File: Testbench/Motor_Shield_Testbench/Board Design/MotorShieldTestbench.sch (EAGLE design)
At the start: 12 parts

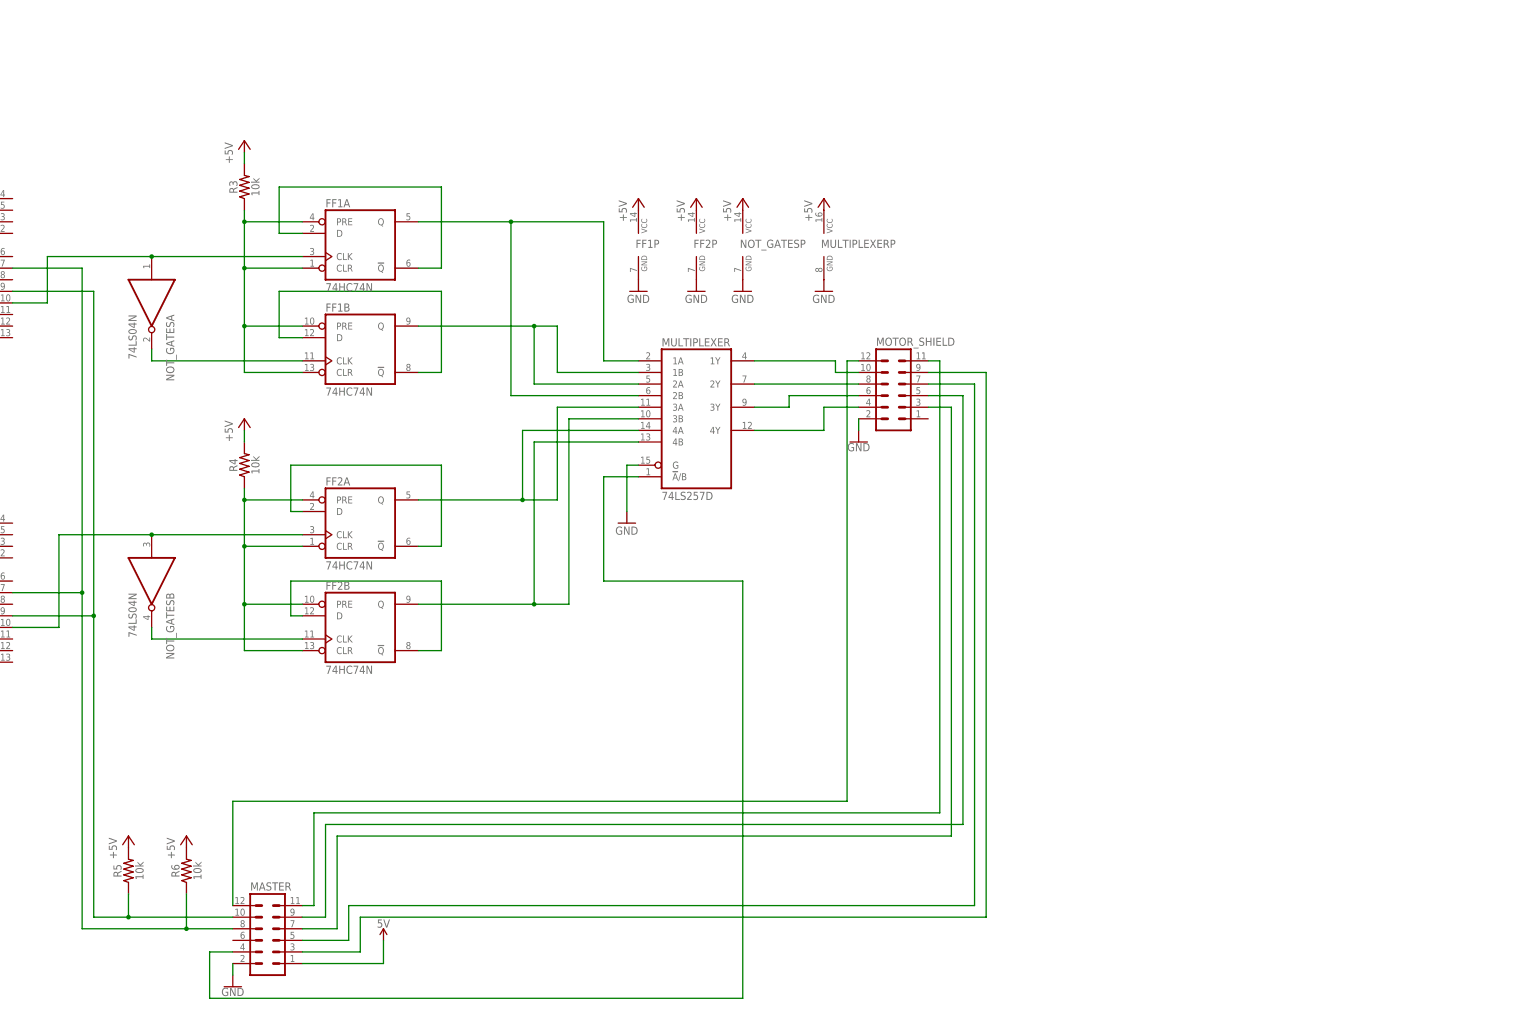
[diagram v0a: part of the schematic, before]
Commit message: board design v2 with complement master pin adjustments
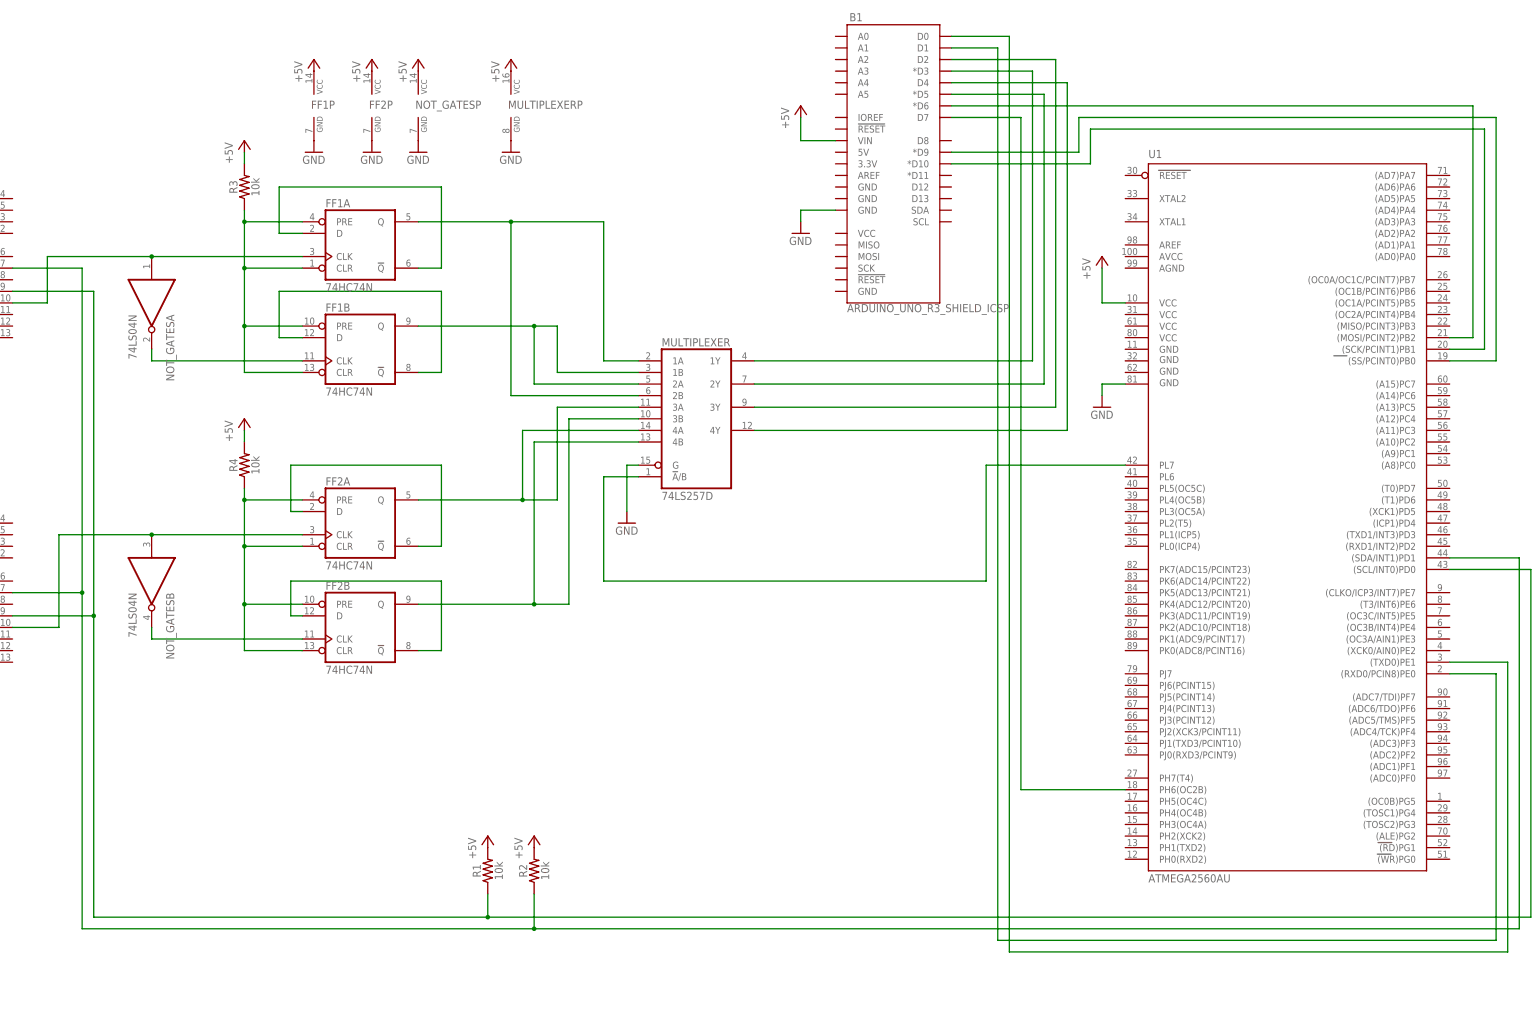
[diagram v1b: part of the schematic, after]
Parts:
- removed MASTER, MOTOR_SHIELD: (no value), con-lstb:MA06-2
- removed R5, R6: 10k, SparkFun-Resistors:10KOHM-HORIZ-1/4W-5%
- added B1: ARDUINO_UNO_R3_SHIELD_ICSP, SparkFun-Boards:ARDUINO_UNO_R3_SHIELD_ICSP
- added R1, R2: 10k, SparkFun-Resistors:10KOHM-HORIZ-1/4W-5%
- added U1: ATMEGA2560AU, SparkFun-IC-Microcontroller:ATMEGA2560AU
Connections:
- removed net 5V: MASTER.1
- removed net N$22: MASTER.7, MOTOR_SHIELD.3
- removed net N$24: MASTER.9, MOTOR_SHIELD.5
- removed net N$25: MASTER.5, MOTOR_SHIELD.7
- removed net N$26: MASTER.3, MOTOR_SHIELD.9
- new net N$28: B1.D0, U1.(TXD0)PE1
- new net N$29: B1.*D9, U1.(SS/PCINT0)PB0
- new net N$30: B1.*D10, U1.(SCK/PCINT1)PB1
- new net N$31: B1.*D6, U1.(MOSI/PCINT2)PB2
- net +5V: now also B1.VIN, R1.2, R2.2, U1.VCC; no longer R5.2, R6.2
- net GND: now also B1.GND@0, U1.GND3; no longer MASTER.2, MOTOR_SHIELD.2
- net N$12: now also B1.D1, U1.(RXD0/PCIN8)PE0; no longer MASTER.11, MOTOR_SHIELD.11
- net N$15: now also B1.*D3; no longer MOTOR_SHIELD.10
- net N$16: now also B1.*D5; no longer MOTOR_SHIELD.8
- net N$17: now also B1.D2; no longer MOTOR_SHIELD.6
- net N$18: now also B1.D4; no longer MOTOR_SHIELD.4
- net N$19: now also R1.1, U1.(SCL/INT0)PD0; no longer MASTER.10, R5.1
- net N$20: now also U1.PL7; no longer MASTER.4
- net N$21: now also R2.1, U1.(SDA/INT1)PD1; no longer MASTER.8, R6.1
- net N$23: now also B1.D7, U1.PH6(OC2B); no longer MASTER.12, MOTOR_SHIELD.12
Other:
- moved on the sheet: FF1P, FF2P, MULTIPLEXERP, NOT_GATESP

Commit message: board design v2
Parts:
- removed ATTINY1, ATTINY2: ATTINY84, SparkFun-IC-Microcontroller:ATTINY84
- added C1, C13, C2, C3, C8: 22pF, SparkFun-Capacitors:22PF-0603-50V-5%
- added C10, C11, C12, C9: 0.1uF, SparkFun-Capacitors:0.1UF-0603-25V-5%
- added C14: 1.0uF, SparkFun-Capacitors:1.0UF-0603-16V-10%
- added C4, C5, C6, C7: 0.1uF, SparkFun-Capacitors:0.1UF-0603-25V-(+80/-20%)
- added LED1, LED2, LED3: (no value), eagle-ltspice:LED_E
- added Q2, Q3: (no value), special:XTAL/S
- added R10, R11, R12, R13: 1k, SparkFun-Resistors:1KOHM-0603-1/10W-1%
- added R5: 27, SparkFun-Resistors:27OHM-0603-1/10W-1%
- added R6: 1M, SparkFun-Resistors:1MOHM-0603-1/4W-5%
- added R7: 10k, SparkFun-Resistors:10KOHM-0603-1/10W-1%
- added R8, R9: 22, SparkFun-Resistors:22OHM-0603-1/10W-1%
- added U2: ATMEGA8U2-AU, Atmel_By_element14_Batch_1-00:ATMEGA8U2-AU
- added U3, U4: ATTINY85-20SU, Atmel_By_element14_Batch_1-00:ATTINY85-20SU
- added X1: MINI-USB-32005-301, con-cypressindustries:MINI-USB-32005-301
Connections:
- new net N$22: R5.1, U1.XTAL1
- new net N$24: C1.2, Q3.1, R5.2
- new net N$25: C2.2, Q3.2, U1.XTAL2
- new net N$26: C8.1, R7.2, U1.RESET
- new net N$32: C3.2, Q2.1, U2.XTAL1
- new net N$33: C13.2, Q2.2, U2.(PC0)_XTAL2
- new net N$34: R9.1, X1.2
- new net N$35: R9.2, U2.D-
- new net N$36: C7.1, U1.AREF
- new net N$37: R8.1, X1.3
- new net N$38: R8.2, U2.D+
- new net N$39: C14.1, U2.UCAP
- new net N$40: R10.2, U2.PD7
- new net N$41: U1.(RXD1/INT2)PD2, U2.PD2
- new net N$42: U1.(TXD1/INT3)PD3, U2.PD3
- new net N$43: LED1.A, R11.2
- new net N$44: LED2.A, R12.2
- new net N$45: LED1.C, U2.PD4
- new net N$46: LED2.C, U2.PD5
- new net N$47: LED3.A, R13.1
- net +5V: now also C10.1, C11.1, C12.1, C4.1, C5.1, C6.1, C9.1, R11.1, R12.1, R13.2, R7.1, U1.AVCC, U1.VCC1, U1.VCC2, U1.VCC3, U2.AVCC, U2.UVCC, U2.VCC, U3.VCC, U4.VCC, X1.1; no longer ATTINY1.VCC, ATTINY2.VCC
- net GND: now also C1.1, C10.2, C11.2, C12.2, C13.1, C14.2, C2.1, C3.1, C4.2, C5.2, C6.2, C7.2, C8.2, C9.2, LED3.C, R10.1, R6.1, R6.2, U1.AGND, U1.GND, U1.GND1, U1.GND2, U2.GND, U2.UGND, U3.GND, U4.GND, X1.5; no longer ATTINY1.GND, ATTINY2.GND
- net N$11: now also U4.PB1; no longer ATTINY2.(PCINT3/T0/ADC3)PA3
- net N$13: now also U3.PB1; no longer ATTINY1.(PCINT3/T0/ADC3)PA3
- net N$19: now also U3.PB2, U4.PB2; no longer ATTINY1.(PCINT4/T1/SCL/USCK/ADC4)PA4, ATTINY2.(PCINT4/T1/SCL/USCK/ADC4)PA4
- net N$21: now also U3.PB0, U4.PB0; no longer ATTINY1.(PCINT6/OC1A/SDA/MOSI/ADC6)PA6, ATTINY2.(PCINT6/OC1A/SDA/MOSI/ADC6)PA6
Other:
- moved on the sheet: FF1P, FF2P, MULTIPLEXERP, NOT_GATESP, U1

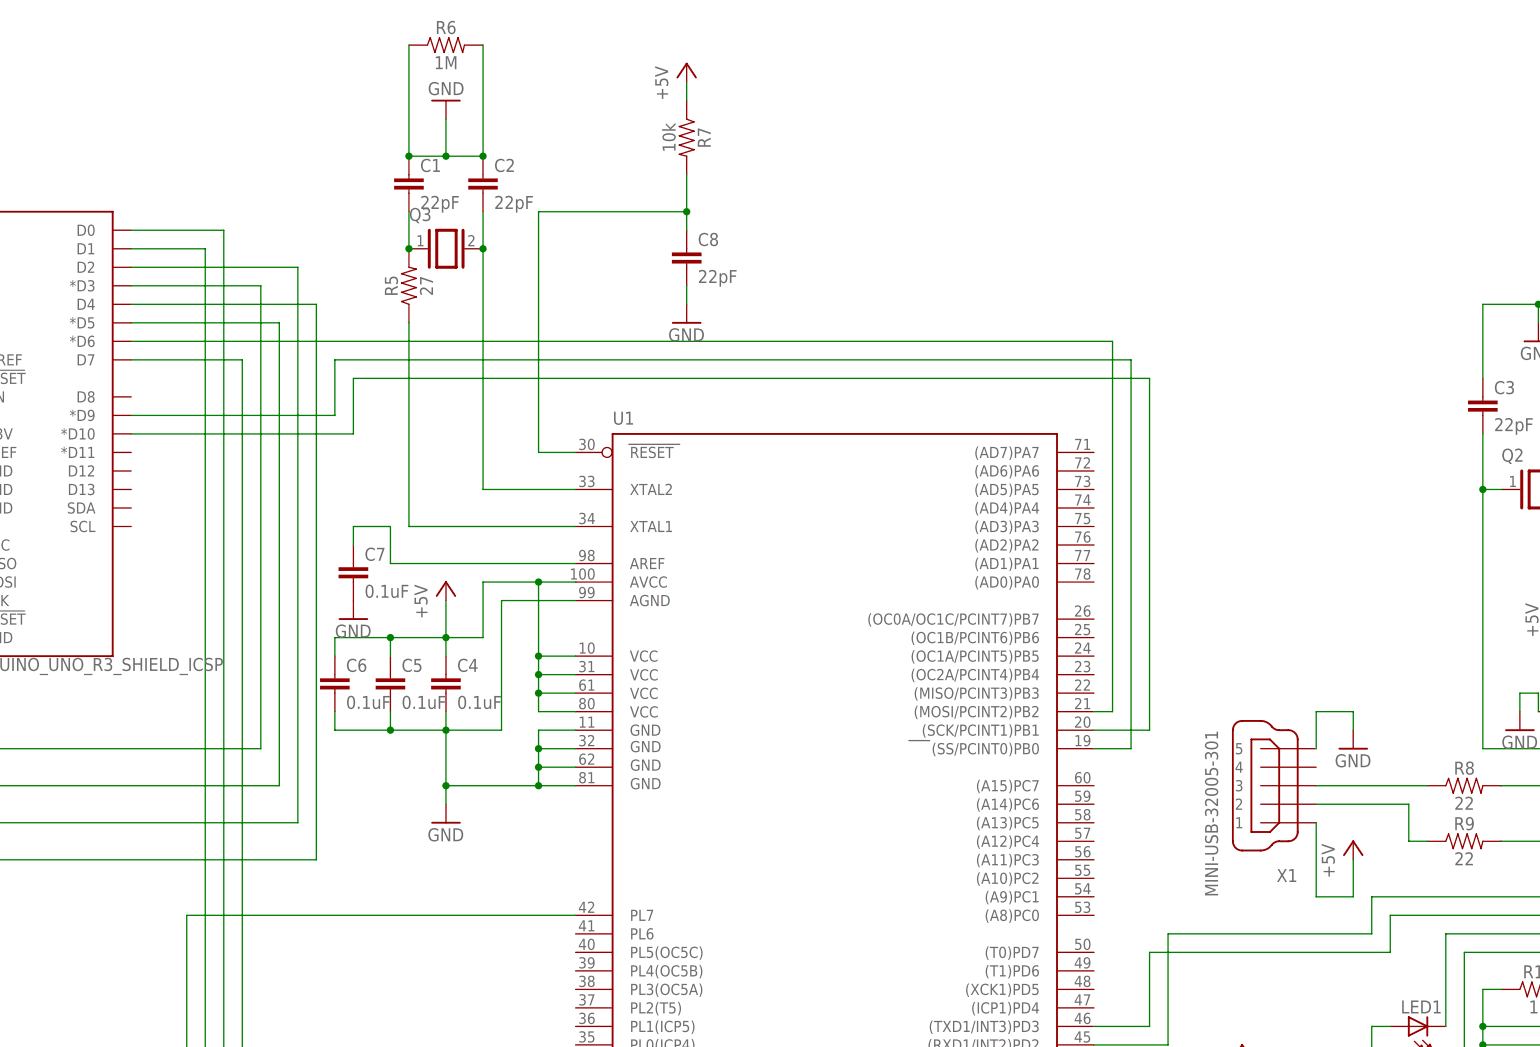
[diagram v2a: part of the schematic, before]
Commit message: added possible serial-to-usb design, minor improvements throughout
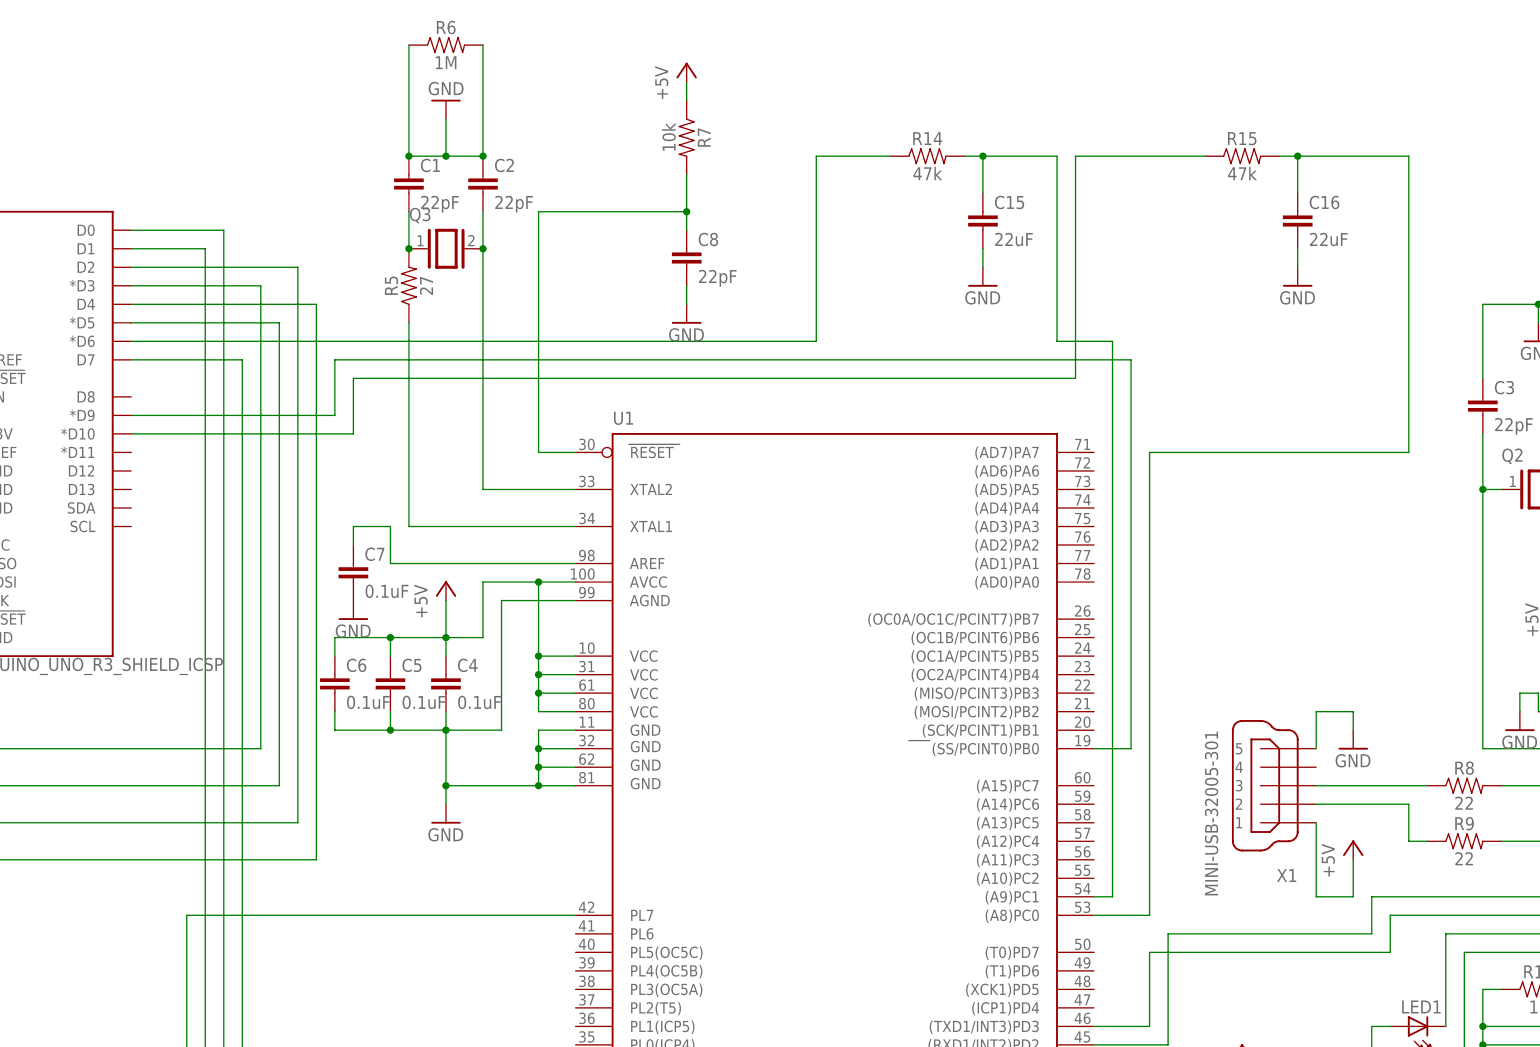
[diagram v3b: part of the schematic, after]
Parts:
- added C15, C16: 22uF, SparkFun-Capacitors:22UF-0805-6.3V-20%
- added R14, R15: 47k, SparkFun-Resistors:47KOHM-0603-1/10W-1%
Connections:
- removed net N$30: B1.*D10, U1.(SCK/PCINT1)PB1
- new net N$48: C15.1, R14.2, U1.(A9)PC1
- new net N$49: B1.*D6, R14.1
- new net N$50: C16.1, R15.2, U1.(A8)PC0
- net GND: now also C15.2, C16.2
- net N$31: now also B1.*D10, R15.1; no longer B1.*D6, U1.(MOSI/PCINT2)PB2
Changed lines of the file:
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@@
 <part name="GND4" library="supply1" deviceset="GND" device=""/>
 <part name="P+6" library="supply1" deviceset="+5V" device=""/>
+<part name="R14" library="SparkFun-Resistors" deviceset="47KOHM" device="-0603-1/10W-1%" value="47k"/>
+<part name="R15" library="SparkFun-Resistors" deviceset="47KOHM" device="-0603-1/10W-1%" value="47k"/>
+<part name="C15" library="SparkFun-Capacitors" deviceset="22UF" device="-0805-6.3V-20%" value="22uF"/>
+<part name="C16" library="SparkFun-Capacitors" deviceset="22UF" device="-0805-6.3V-20%" value="22uF"/>
+<part name="GND17" library="supply1" deviceset="GND" device=""/>
+<part name="GND19" library="supply1" deviceset="GND" device=""/>
 </parts>
 <sheets>
@@
 <instance part="GND4" gate="1" x="-55.88" y="-35.56"/>
 <instance part="P+6" gate="1" x="-55.88" y="-10.16"/>
+<instance part="R14" gate="G$1" x="314.96" y="144.78"/>
+<instance part="R15" gate="G$1" x="358.14" y="144.78"/>
+<instance part="C15" gate="G$1" x="322.58" y="134.62"/>
+<instance part="C16" gate="G$1" x="365.76" y="134.62"/>
+<instance part="GND17" gate="1" x="322.58" y="127"/>
+<instance part="GND19" gate="1" x="365.76" y="127"/>
 </instances>
 <busses>
@@
 <wire x1="-55.88" y1="-27.94" x2="-50.8" y2="-27.94" width="0.1524" layer="91"/>
 </segment>
+<segment>
+<pinref part="C16" gate="G$1" pin="2"/>
+<pinref part="GND19" gate="1" pin="GND"/>
+<wire x1="365.76" y1="132.08" x2="365.76" y2="129.54" width="0.1524" layer="91"/>
+</segment>
+<segment>
+<pinref part="C15" gate="G$1" pin="2"/>
+<pinref part="GND17" gate="1" pin="GND"/>
+<wire x1="322.58" y1="132.08" x2="322.58" y2="129.54" width="0.1524" layer="91"/>
+</segment>
 </net>
 <net name="N$19" class="0">
@@
 </segment>
 </net>
-<net name="N$30" class="0">
-<segment>
-<pinref part="U1" gate="1" pin="(SCK/PCINT1)PB1"/>
-<wire x1="345.44" y1="114.3" x2="236.22" y2="114.3" width="0.1524" layer="91"/>
-<wire x1="236.22" y1="114.3" x2="236.22" y2="106.68" width="0.1524" layer="91"/>
-<pinref part="B1" gate="G$1" pin="*D10"/>
-<wire x1="236.22" y1="106.68" x2="205.74" y2="106.68" width="0.1524" layer="91"/>
-<wire x1="345.44" y1="114.3" x2="345.44" y2="66.04" width="0.1524" layer="91"/>
-<wire x1="345.44" y1="66.04" x2="337.82" y2="66.04" width="0.1524" layer="91"/>
-</segment>
-</net>
-<net name="N$31" class="0">
-<segment>
-<pinref part="U1" gate="1" pin="(MOSI/PCINT2)PB2"/>
-<pinref part="B1" gate="G$1" pin="*D6"/>
-<wire x1="340.36" y1="119.38" x2="205.74" y2="119.38" width="0.1524" layer="91"/>
-<wire x1="340.36" y1="119.38" x2="340.36" y2="68.58" width="0.1524" layer="91"/>
-<wire x1="340.36" y1="68.58" x2="337.82" y2="68.58" width="0.1524" layer="91"/>
-</segment>
-</net>
 <net name="N$15" class="0">
 <segment>
@@
 </segment>
 </net>
+<net name="N$48" class="0">
+<segment>
+<pinref part="R14" gate="G$1" pin="2"/>
+<pinref part="C15" gate="G$1" pin="1"/>
+<wire x1="320.04" y1="144.78" x2="322.58" y2="144.78" width="0.1524" layer="91"/>
+<wire x1="322.58" y1="144.78" x2="322.58" y2="139.7" width="0.1524" layer="91"/>
+<wire x1="340.36" y1="119.38" x2="332.74" y2="119.38" width="0.1524" layer="91"/>
+<wire x1="340.36" y1="119.38" x2="340.36" y2="43.18" width="0.1524" layer="91"/>
+<pinref part="U1" gate="1" pin="(A9)PC1"/>
+<wire x1="340.36" y1="43.18" x2="337.82" y2="43.18" width="0.1524" layer="91"/>
+<wire x1="322.58" y1="144.78" x2="332.74" y2="144.78" width="0.1524" layer="91"/>
+<wire x1="332.74" y1="144.78" x2="332.74" y2="119.38" width="0.1524" layer="91"/>
+<junction x="322.58" y="144.78"/>
+</segment>
+</net>
+<net name="N$49" class="0">
+<segment>
+<pinref part="B1" gate="G$1" pin="*D6"/>
+<pinref part="R14" gate="G$1" pin="1"/>
+<wire x1="299.72" y1="144.78" x2="309.88" y2="144.78" width="0.1524" layer="91"/>
+<wire x1="299.72" y1="119.38" x2="299.72" y2="144.78" width="0.1524" layer="91"/>
+<wire x1="299.72" y1="119.38" x2="205.74" y2="119.38" width="0.1524" layer="91"/>
+</segment>
+</net>
+<net name="N$31" class="0">
+<segment>
+<wire x1="335.28" y1="114.3" x2="236.22" y2="114.3" width="0.1524" layer="91"/>
+<wire x1="236.22" y1="114.3" x2="236.22" y2="106.68" width="0.1524" layer="91"/>
+<pinref part="B1" gate="G$1" pin="*D10"/>
+<wire x1="236.22" y1="106.68" x2="205.74" y2="106.68" width="0.1524" layer="91"/>
+<wire x1="335.28" y1="114.3" x2="335.28" y2="144.78" width="0.1524" layer="91"/>
+<pinref part="R15" gate="G$1" pin="1"/>
+<wire x1="335.28" y1="144.78" x2="353.06" y2="144.78" width="0.1524" layer="91"/>
+</segment>
+</net>
+<net name="N$50" class="0">
+<segment>
+<pinref part="U1" gate="1" pin="(A8)PC0"/>
+<wire x1="345.44" y1="40.64" x2="337.82" y2="40.64" width="0.1524" layer="91"/>
+<wire x1="345.44" y1="104.14" x2="345.44" y2="40.64" width="0.1524" layer="91"/>
+<wire x1="381" y1="104.14" x2="345.44" y2="104.14" width="0.1524" layer="91"/>
+<wire x1="381" y1="144.78" x2="381" y2="104.14" width="0.1524" layer="91"/>
+<pinref part="C16" gate="G$1" pin="1"/>
+<wire x1="365.76" y1="144.78" x2="365.76" y2="139.7" width="0.1524" layer="91"/>
+<wire x1="365.76" y1="144.78" x2="381" y2="144.78" width="0.1524" layer="91"/>
+<junction x="365.76" y="144.78"/>
+<pinref part="R15" gate="G$1" pin="2"/>
+<wire x1="363.22" y1="144.78" x2="365.76" y2="144.78" width="0.1524" layer="91"/>
+</segment>
+</net>
